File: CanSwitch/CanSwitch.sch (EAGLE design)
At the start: 6 parts

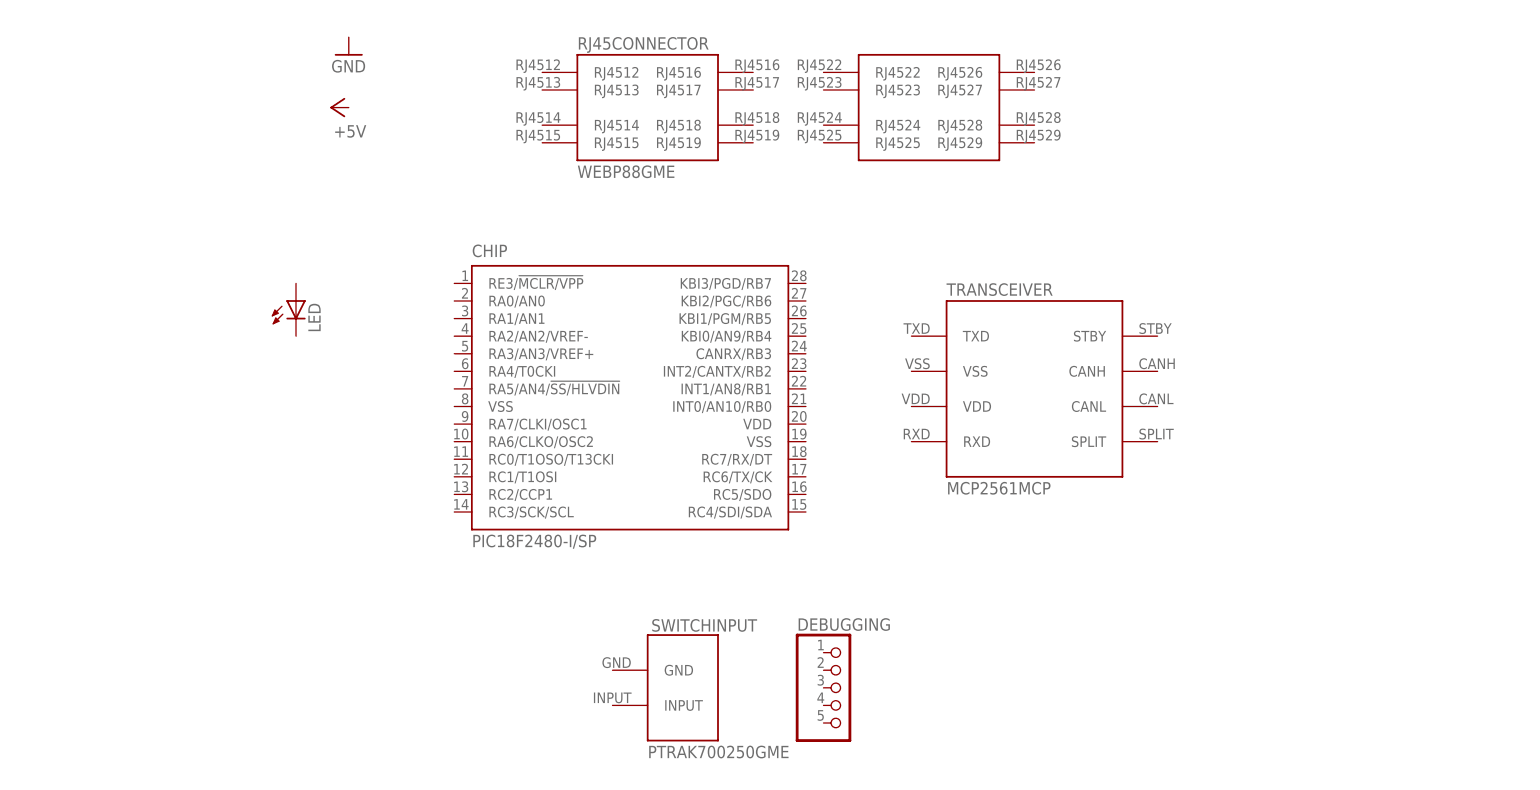
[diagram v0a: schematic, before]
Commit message: wiring all up, done all in the switch with the exception of wiring up RJ45 to the rest
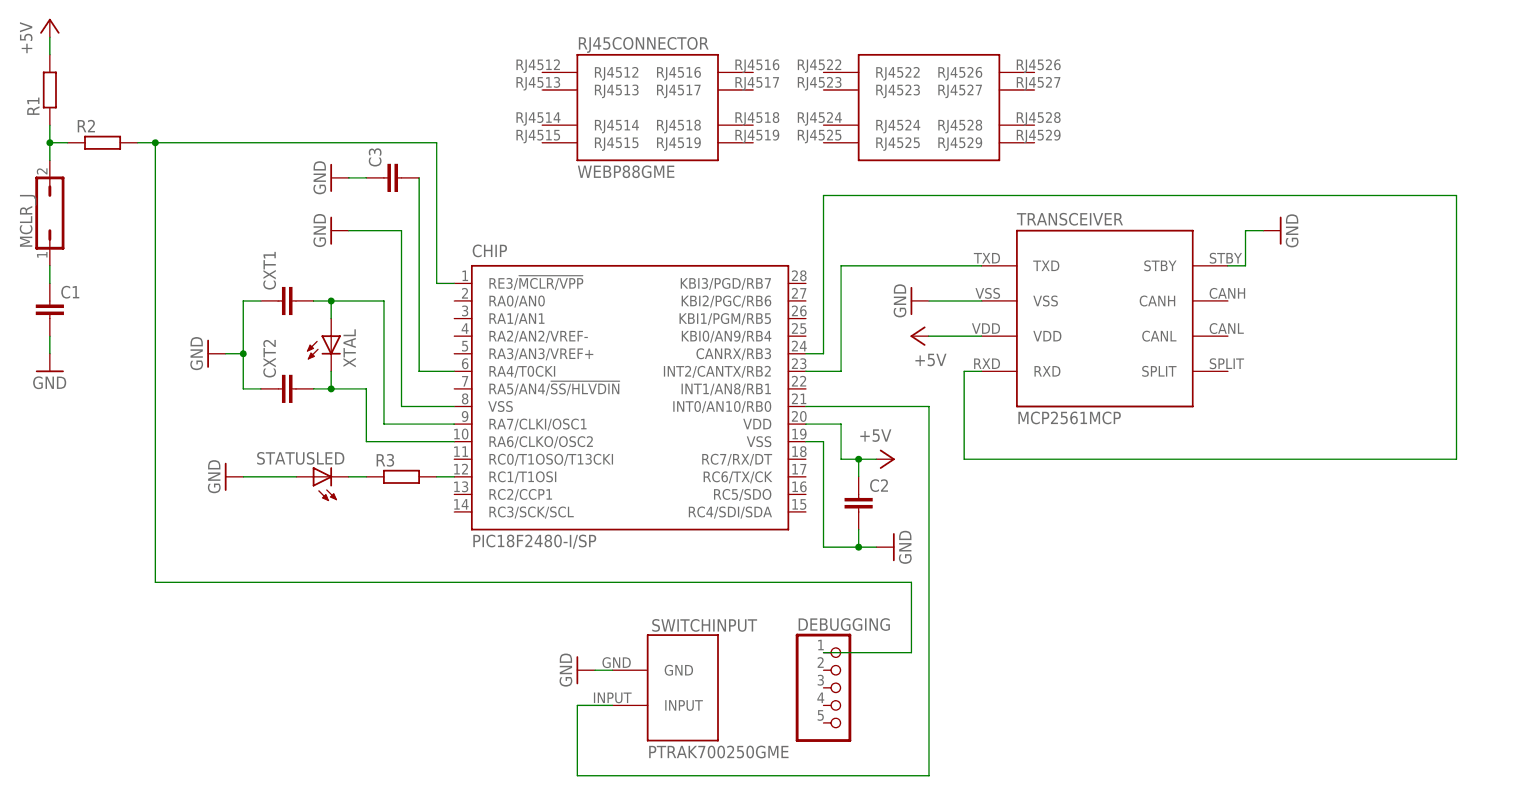
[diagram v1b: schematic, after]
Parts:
- removed LED: (no value), led:LED5MM
- added C1, C2, C3, CXT1, CXT2: (no value), rcl:C-EUC0805
- added MCLR_J: (no value), jumper:JP1Q
- added R1, R2, R3: (no value), rcl:R-EU_0207/10
- added STATUSLED, XTAL: (no value), led:LED5MM
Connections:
- new net +5V: C2.1, CHIP.VDD, R1.2, TRANSCEIVER.VDD
- new net GND: C1.2, C2.2, C3.1, CHIP.VSS, CHIP.VSS@1, CXT1.1, CXT2.1, STATUSLED.A, SWITCHINPUT.GND, TRANSCEIVER.STBY, TRANSCEIVER.VSS
- new net N$1: C1.1, MCLR_J.1
- new net N$10: CHIP.INT2/CANTX/RB2, TRANSCEIVER.TXD
- new net N$11: CHIP.CANRX/RB3, TRANSCEIVER.RXD
- new net N$2: MCLR_J.2, R1.1, R2.1
- new net N$3: CHIP.RE3/!MCLR/VPP, DEBUGGING.1, R2.2
- new net N$4: C3.2, CHIP.RA4/T0CKI
- new net N$5: CHIP.RA6/CLKO/OSC2, CXT2.2, XTAL.C
- new net N$6: CHIP.RA7/CLKI/OSC1, CXT1.2, XTAL.A
- new net N$7: CHIP.RC1/T1OSI, R3.2
- new net N$8: R3.1, STATUSLED.C
- new net N$9: CHIP.INT0/AN10/RB0, SWITCHINPUT.INPUT
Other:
- moved on the sheet: TRANSCEIVER

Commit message: wired up all together, no resistor or capacitor added to switch board just yet, won't be here. Now can move to PCB
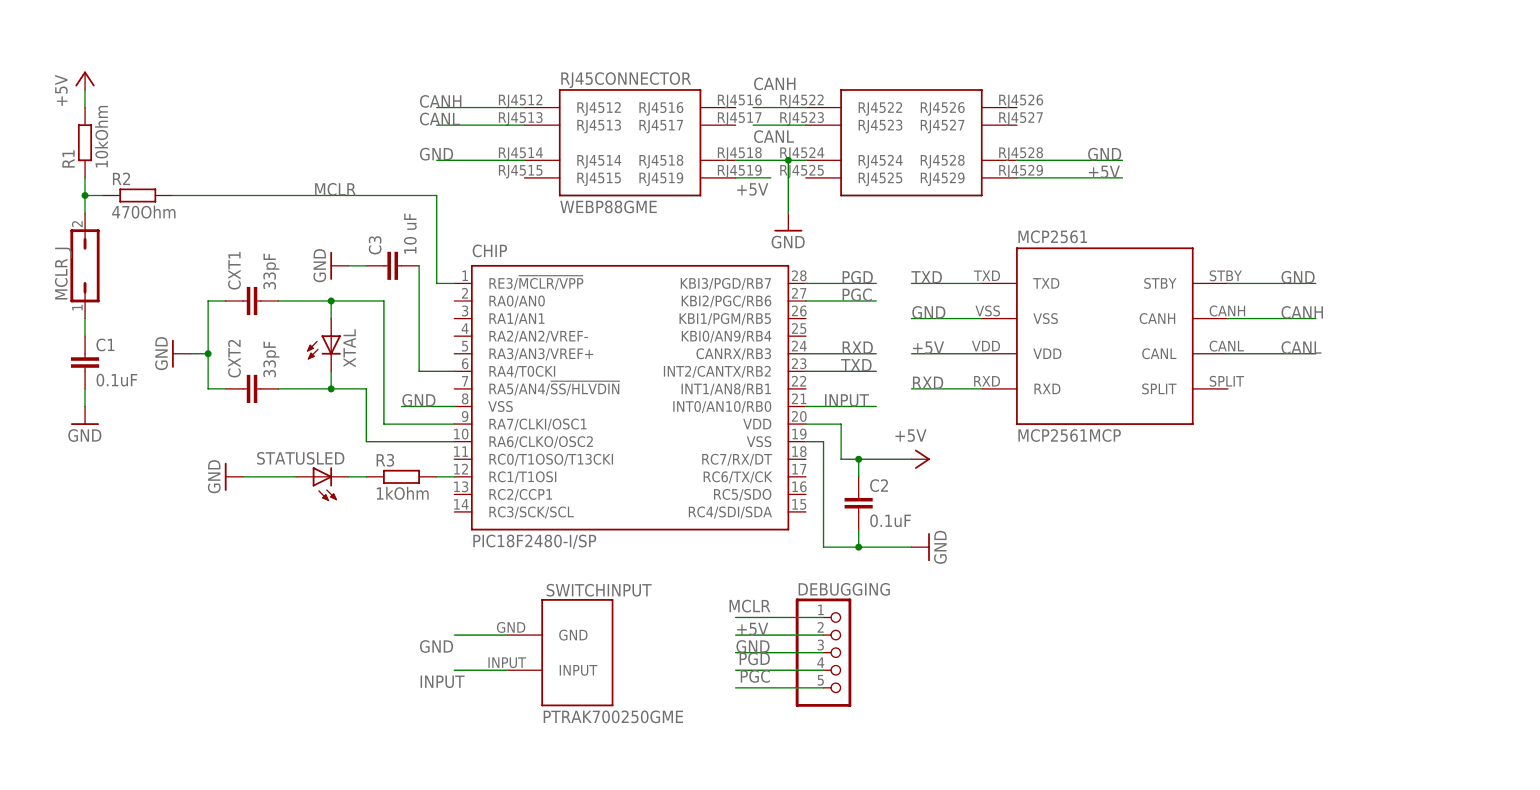
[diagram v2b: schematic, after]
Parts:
- removed TRANSCEIVER: MCP2561MCP, PoJD:MCP2561MCP
- added MCP2561: MCP2561MCP, PoJD:MCP2561MCP
- C1, C2: value (none) -> 0.1uF
- C3: value (none) -> 10 uF
- CXT1, CXT2: value (none) -> 33pF
- R1: value (none) -> 10kOhm
- R2: value (none) -> 470Ohm
- R3: value (none) -> 1kOhm
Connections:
- net N$3 renamed MCLR
- net N$9 renamed INPUT
- removed net N$10: CHIP.INT2/CANTX/RB2, TRANSCEIVER.TXD
- removed net N$11: CHIP.CANRX/RB3, TRANSCEIVER.RXD
- new net CANH: MCP2561.CANH, RJ45CONNECTOR.RJ4512, RJ45CONNECTOR.RJ4522
- new net CANL: MCP2561.CANL, RJ45CONNECTOR.RJ4513, RJ45CONNECTOR.RJ4523
- new net PGC: CHIP.KBI2/PGC/RB6, DEBUGGING.5
- new net PGD: CHIP.KBI3/PGD/RB7, DEBUGGING.4
- new net RXD: CHIP.CANRX/RB3, MCP2561.RXD
- new net TXD: CHIP.INT2/CANTX/RB2, MCP2561.TXD
- net +5V: now also DEBUGGING.2, MCP2561.VDD, RJ45CONNECTOR.RJ4519, RJ45CONNECTOR.RJ4529; no longer TRANSCEIVER.VDD
- net GND: now also DEBUGGING.3, MCP2561.STBY, MCP2561.VSS, RJ45CONNECTOR.RJ4514, RJ45CONNECTOR.RJ4518, RJ45CONNECTOR.RJ4524, RJ45CONNECTOR.RJ4528; no longer TRANSCEIVER.STBY, TRANSCEIVER.VSS
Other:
- moved on the sheet: C1, C3, CXT1, CXT2, DEBUGGING, MCLR_J, R1, R2, RJ45CONNECTOR, SWITCHINPUT

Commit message: little edits to the schema - adding capacitors to each pair of VDD and VSS, creating first version of PCB. Missing box and proper wiring up
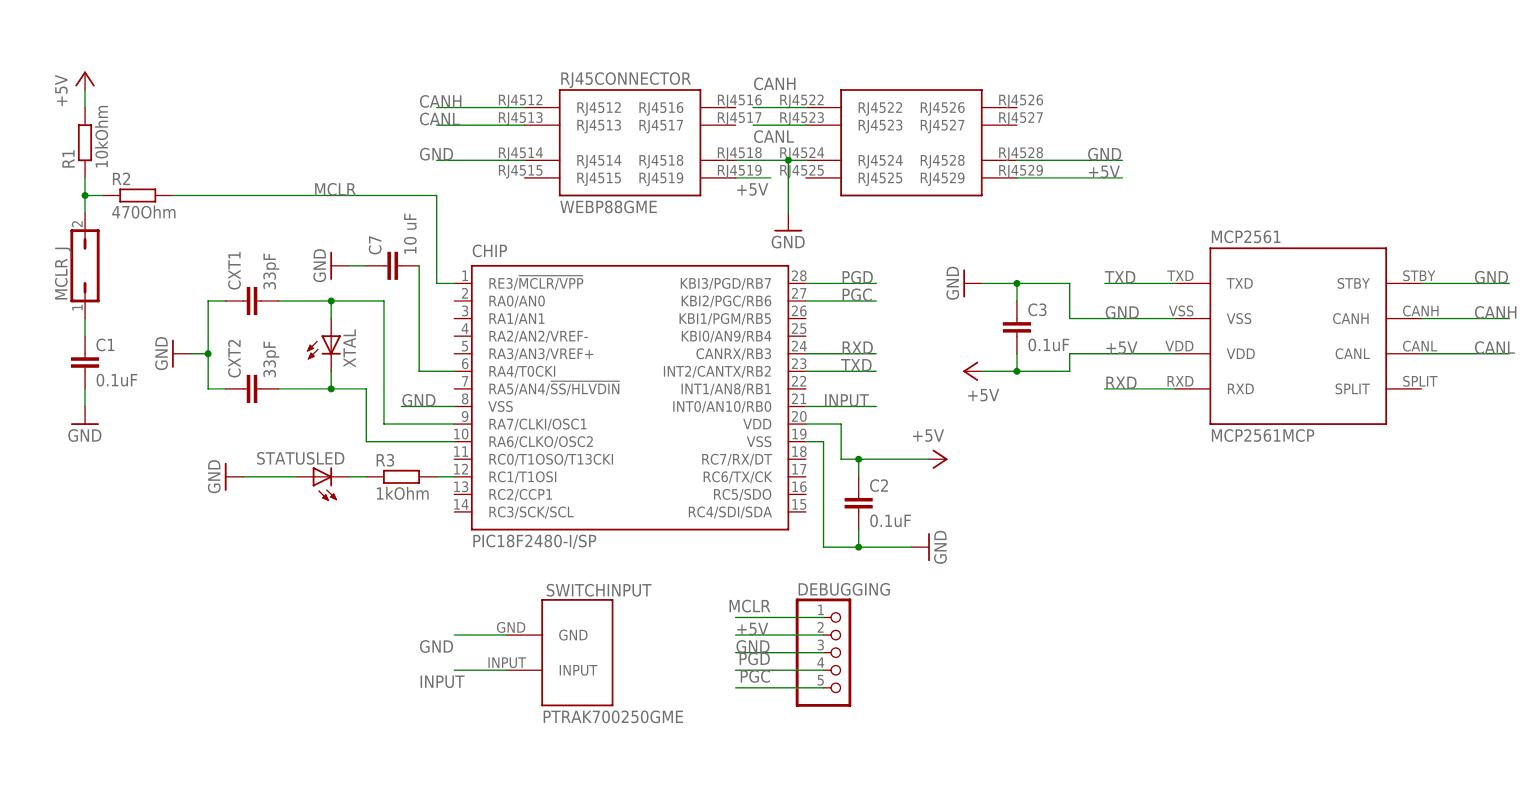
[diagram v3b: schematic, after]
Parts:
- added C7: 10 uF, rcl:C-EUC0805
- C3: value 10 uF -> 0.1uF
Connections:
- net +5V: now also C3.2
- net GND: now also C7.1
- net N$4: now also C7.2; no longer C3.2
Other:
- moved on the sheet: C3, MCP2561
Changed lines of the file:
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@@
 <part name="P+3" library="supply1" deviceset="+5V" device=""/>
 <part name="C2" library="rcl" deviceset="C-EU" device="C0805" value="0.1uF"/>
-<part name="C3" library="rcl" deviceset="C-EU" device="C0805" value="10 uF"/>
+<part name="C7" library="rcl" deviceset="C-EU" device="C0805" value="10 uF"/>
 <part name="GND5" library="supply1" deviceset="GND" device=""/>
 <part name="XTAL" library="led" deviceset="LED" device="5MM"/>
@@
 <part name="GND7" library="supply1" deviceset="GND" device=""/>
 <part name="GND1" library="supply1" deviceset="GND" device=""/>
+<part name="P+1" library="supply1" deviceset="+5V" device=""/>
+<part name="GND3" library="supply1" deviceset="GND" device=""/>
+<part name="C3" library="rcl" deviceset="C-EU" device="C0805" value="0.1uF"/>
 </parts>
 <sheets>
@@
 <instance part="RJ45CONNECTOR" gate="G$1" x="-55.88" y="124.46"/>
 <instance part="SWITCHINPUT" gate="G$1" x="-83.82" y="50.8"/>
-<instance part="MCP2561" gate="G$1" x="-7.62" y="96.52"/>
+<instance part="MCP2561" gate="G$1" x="20.32" y="96.52"/>
 <instance part="MCLR_J" gate="A" x="-154.94" y="106.68"/>
 <instance part="R1" gate="G$1" x="-154.94" y="124.46" rot="R90"/>
@@
 <instance part="C1" gate="G$1" x="-154.94" y="93.98"/>
 <instance part="GND4" gate="1" x="-33.02" y="66.04" rot="R90"/>
-<instance part="P+3" gate="1" x="-33.02" y="78.74" rot="R270"/>
+<instance part="P+3" gate="1" x="-30.48" y="78.74" rot="R270"/>
 <instance part="C2" gate="G$1" x="-43.18" y="73.66"/>
-<instance part="C3" gate="G$1" x="-111.76" y="106.68" rot="R90"/>
+<instance part="C7" gate="G$1" x="-111.76" y="106.68" rot="R90"/>
 <instance part="GND5" gate="1" x="-119.38" y="106.68" rot="R270"/>
 <instance part="XTAL" gate="G$1" x="-119.38" y="96.52"/>
@@
 <instance part="GND7" gate="1" x="-134.62" y="76.2" rot="R270"/>
 <instance part="GND1" gate="1" x="-53.34" y="111.76"/>
+<instance part="P+1" gate="1" x="-27.94" y="91.44" rot="R90"/>
+<instance part="GND3" gate="1" x="-27.94" y="104.14" rot="R270"/>
+<instance part="C3" gate="G$1" x="-20.32" y="99.06"/>
 </instances>
 <busses>
@@
 <wire x1="-45.72" y1="78.74" x2="-43.18" y2="78.74" width="0.1524" layer="91"/>
 <pinref part="C2" gate="G$1" pin="1"/>
-<wire x1="-43.18" y1="78.74" x2="-35.56" y2="78.74" width="0.1524" layer="91"/>
+<wire x1="-43.18" y1="78.74" x2="-33.02" y2="78.74" width="0.1524" layer="91"/>
 <wire x1="-43.18" y1="76.2" x2="-43.18" y2="78.74" width="0.1524" layer="91"/>
 <junction x="-43.18" y="78.74"/>
@@
 <segment>
 <pinref part="MCP2561" gate="G$1" pin="VDD"/>
-<wire x1="-35.56" y1="93.98" x2="-25.4" y2="93.98" width="0.1524" layer="91"/>
-<label x="-35.56" y="93.98" size="1.778" layer="95"/>
+<wire x1="-12.7" y1="93.98" x2="2.54" y2="93.98" width="0.1524" layer="91"/>
+<label x="-7.62" y="93.98" size="1.778" layer="95"/>
+<wire x1="-12.7" y1="93.98" x2="-12.7" y2="91.44" width="0.1524" layer="91"/>
+<pinref part="P+1" gate="1" pin="+5V"/>
+<wire x1="-12.7" y1="91.44" x2="-20.32" y2="91.44" width="0.1524" layer="91"/>
+<pinref part="C3" gate="G$1" pin="2"/>
+<wire x1="-20.32" y1="91.44" x2="-25.4" y2="91.44" width="0.1524" layer="91"/>
+<wire x1="-20.32" y1="93.98" x2="-20.32" y2="91.44" width="0.1524" layer="91"/>
+<junction x="-20.32" y="91.44"/>
 </segment>
 <segment>
@@
 </segment>
 <segment>
-<pinref part="C3" gate="G$1" pin="1"/>
+<pinref part="C7" gate="G$1" pin="1"/>
 <pinref part="GND5" gate="1" pin="GND"/>
 <wire x1="-114.3" y1="106.68" x2="-116.84" y2="106.68" width="0.1524" layer="91"/>
@@
 <segment>
 <pinref part="MCP2561" gate="G$1" pin="VSS"/>
-<wire x1="-25.4" y1="99.06" x2="-35.56" y2="99.06" width="0.1524" layer="91"/>
-<label x="-35.56" y="99.06" size="1.778" layer="95"/>
+<wire x1="2.54" y1="99.06" x2="-12.7" y2="99.06" width="0.1524" layer="91"/>
+<label x="-7.62" y="99.06" size="1.778" layer="95"/>
+<wire x1="-12.7" y1="99.06" x2="-12.7" y2="104.14" width="0.1524" layer="91"/>
+<pinref part="GND3" gate="1" pin="GND"/>
+<wire x1="-12.7" y1="104.14" x2="-20.32" y2="104.14" width="0.1524" layer="91"/>
+<pinref part="C3" gate="G$1" pin="1"/>
+<wire x1="-20.32" y1="104.14" x2="-25.4" y2="104.14" width="0.1524" layer="91"/>
+<wire x1="-20.32" y1="101.6" x2="-20.32" y2="104.14" width="0.1524" layer="91"/>
+<junction x="-20.32" y="104.14"/>
 </segment>
 <segment>
 <pinref part="MCP2561" gate="G$1" pin="STBY"/>
-<wire x1="10.16" y1="104.14" x2="22.86" y2="104.14" width="0.1524" layer="91"/>
-<label x="17.78" y="104.14" size="1.778" layer="95"/>
+<wire x1="38.1" y1="104.14" x2="50.8" y2="104.14" width="0.1524" layer="91"/>
+<label x="45.72" y="104.14" size="1.778" layer="95"/>
 </segment>
 <segment>
@@
 <pinref part="CHIP" gate="G$1" pin="RA4/T0CKI"/>
 <wire x1="-101.6" y1="91.44" x2="-106.68" y2="91.44" width="0.1524" layer="91"/>
-<pinref part="C3" gate="G$1" pin="2"/>
+<pinref part="C7" gate="G$1" pin="2"/>
 <wire x1="-106.68" y1="91.44" x2="-106.68" y2="106.68" width="0.1524" layer="91"/>
 </segment>
@@
 <segment>
 <pinref part="MCP2561" gate="G$1" pin="CANH"/>
-<wire x1="10.16" y1="99.06" x2="22.86" y2="99.06" width="0.1524" layer="91"/>
-<label x="17.78" y="99.06" size="1.778" layer="95"/>
+<wire x1="38.1" y1="99.06" x2="50.8" y2="99.06" width="0.1524" layer="91"/>
+<label x="45.72" y="99.06" size="1.778" layer="95"/>
 </segment>
 <segment>
@@
 <segment>
 <pinref part="MCP2561" gate="G$1" pin="CANL"/>
-<wire x1="10.16" y1="93.98" x2="22.86" y2="93.98" width="0.1524" layer="91"/>
-<label x="17.78" y="93.98" size="1.778" layer="95"/>
+<wire x1="38.1" y1="93.98" x2="50.8" y2="93.98" width="0.1524" layer="91"/>
+<label x="45.72" y="93.98" size="1.778" layer="95"/>
 </segment>
 <segment>
@@
 <segment>
 <pinref part="MCP2561" gate="G$1" pin="TXD"/>
-<wire x1="-25.4" y1="104.14" x2="-35.56" y2="104.14" width="0.1524" layer="91"/>
-<label x="-35.56" y="104.14" size="1.778" layer="95"/>
+<wire x1="2.54" y1="104.14" x2="-7.62" y2="104.14" width="0.1524" layer="91"/>
+<label x="-7.62" y="104.14" size="1.778" layer="95"/>
 </segment>
 <segment>
@@
 <segment>
 <pinref part="MCP2561" gate="G$1" pin="RXD"/>
-<wire x1="-25.4" y1="88.9" x2="-35.56" y2="88.9" width="0.1524" layer="91"/>
-<label x="-35.56" y="88.9" size="1.778" layer="95"/>
-</segment>
-<segment>
+<wire x1="2.54" y1="88.9" x2="-7.62" y2="88.9" width="0.1524" layer="91"/>
+<label x="-7.62" y="88.9" size="1.778" layer="95"/>
+</segment>
+<segment>

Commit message: first attempt to do proper wiring on the board
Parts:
- XTAL: value (none) -> 16MHz; device led:LED5MM -> special:XTAL/S
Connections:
- removed net N$5: CHIP.RA6/CLKO/OSC2, CXT2.2, XTAL.C
- new net N$3: CHIP.RA6/CLKO/OSC2, CXT2.2, XTAL.1
- net N$6: now also XTAL.2; no longer XTAL.A
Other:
- moved on the sheet: CXT2
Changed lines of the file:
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@@
 <part name="C7" library="rcl" deviceset="C-EU" device="C0805" value="10 uF"/>
 <part name="GND5" library="supply1" deviceset="GND" device=""/>
-<part name="XTAL" library="led" deviceset="LED" device="5MM"/>
 <part name="CXT1" library="rcl" deviceset="C-EU" device="C0805" value="33pF"/>
 <part name="CXT2" library="rcl" deviceset="C-EU" device="C0805" value="33pF"/>
@@
 <part name="GND3" library="supply1" deviceset="GND" device=""/>
 <part name="C3" library="rcl" deviceset="C-EU" device="C0805" value="0.1uF"/>
+<part name="XTAL" library="special" deviceset="XTAL/S" device="" value="16MHz"/>
 </parts>
 <sheets>
@@
 <instance part="C7" gate="G$1" x="-111.76" y="106.68" rot="R90"/>
 <instance part="GND5" gate="1" x="-119.38" y="106.68" rot="R270"/>
-<instance part="XTAL" gate="G$1" x="-119.38" y="96.52"/>
 <instance part="CXT1" gate="G$1" x="-132.08" y="101.6" rot="R90"/>
-<instance part="CXT2" gate="G$1" x="-132.08" y="88.9" rot="R90"/>
+<instance part="CXT2" gate="G$1" x="-132.08" y="86.36" rot="R90"/>
 <instance part="GND6" gate="1" x="-142.24" y="93.98" rot="R270"/>
 <instance part="R3" gate="G$1" x="-109.22" y="76.2"/>
@@
 <instance part="GND3" gate="1" x="-27.94" y="104.14" rot="R270"/>
 <instance part="C3" gate="G$1" x="-20.32" y="99.06"/>
+<instance part="XTAL" gate="G$1" x="-119.38" y="93.98" rot="R90"/>
 </instances>
 <busses>
@@
 <segment>
 <pinref part="CXT2" gate="G$1" pin="1"/>
-<wire x1="-134.62" y1="88.9" x2="-137.16" y2="88.9" width="0.1524" layer="91"/>
+<wire x1="-134.62" y1="86.36" x2="-137.16" y2="88.9" width="0.1524" layer="91"/>
 <wire x1="-137.16" y1="88.9" x2="-137.16" y2="93.98" width="0.1524" layer="91"/>
 <pinref part="GND6" gate="1" pin="GND"/>
@@
 <pinref part="CXT1" gate="G$1" pin="2"/>
 <wire x1="-111.76" y1="101.6" x2="-119.38" y2="101.6" width="0.1524" layer="91"/>
-<pinref part="XTAL" gate="G$1" pin="A"/>
+<pinref part="XTAL" gate="G$1" pin="2"/>
 <wire x1="-119.38" y1="101.6" x2="-127" y2="101.6" width="0.1524" layer="91"/>
 <wire x1="-119.38" y1="99.06" x2="-119.38" y2="101.6" width="0.1524" layer="91"/>
@@
 </segment>
 </net>
-<net name="N$5" class="0">
-<segment>
-<pinref part="CHIP" gate="G$1" pin="RA6/CLKO/OSC2"/>
-<wire x1="-101.6" y1="81.28" x2="-114.3" y2="81.28" width="0.1524" layer="91"/>
-<wire x1="-114.3" y1="81.28" x2="-114.3" y2="88.9" width="0.1524" layer="91"/>
-<pinref part="CXT2" gate="G$1" pin="2"/>
-<wire x1="-114.3" y1="88.9" x2="-119.38" y2="88.9" width="0.1524" layer="91"/>
-<pinref part="XTAL" gate="G$1" pin="C"/>
-<wire x1="-119.38" y1="88.9" x2="-127" y2="88.9" width="0.1524" layer="91"/>
-<wire x1="-119.38" y1="91.44" x2="-119.38" y2="88.9" width="0.1524" layer="91"/>
-<junction x="-119.38" y="88.9"/>
-</segment>
-</net>
 <net name="N$7" class="0">
 <segment>
@@
 </segment>
 </net>
+<net name="N$3" class="0">
+<segment>
+<pinref part="CHIP" gate="G$1" pin="RA6/CLKO/OSC2"/>
+<wire x1="-101.6" y1="81.28" x2="-114.3" y2="81.28" width="0.1524" layer="91"/>
+<wire x1="-114.3" y1="81.28" x2="-114.3" y2="86.36" width="0.1524" layer="91"/>
+<pinref part="CXT2" gate="G$1" pin="2"/>
+<wire x1="-114.3" y1="86.36" x2="-119.38" y2="86.36" width="0.1524" layer="91"/>
+<pinref part="XTAL" gate="G$1" pin="1"/>
+<wire x1="-119.38" y1="86.36" x2="-127" y2="86.36" width="0.1524" layer="91"/>
+<wire x1="-119.38" y1="88.9" x2="-119.38" y2="86.36" width="0.1524" layer="91"/>
+<junction x="-119.38" y="86.36"/>
+</segment>
+</net>
